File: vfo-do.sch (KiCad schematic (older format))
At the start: 23 parts, among them P1 12V in, P2 DWN, P3 Si5351, P4 Encoder, P5 GPS, P6 UP, P7 Band, P8 Reset, U1 24AA02-OT, U2 LM7808_TO220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

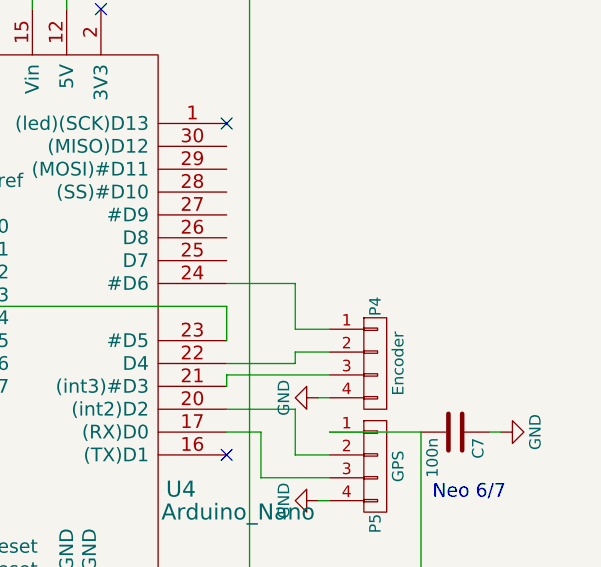
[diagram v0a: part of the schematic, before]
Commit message: Add GPS switchoff button
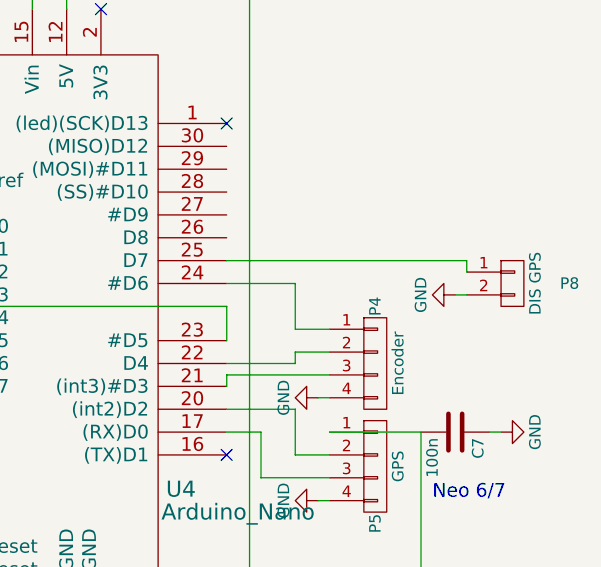
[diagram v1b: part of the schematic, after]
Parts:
- added P8: DIS GPS, Connectors_Molex:Molex_KK-6410-02_02x2.54mm_Straight, symbol vfo-do-rescue:CONN_01X02
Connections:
- net GND: now also P8.2 (P2)
- net at U4.25 (D7): now also P8.1 (P1)
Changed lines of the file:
@@
 Wire Wire Line
 	5800 750  6450 750
+Wire Wire Line
+	9000 3850 9050 3850
+$Comp
+L vfo-do-rescue:CONN_01X02 P8
+U 1 1 613FBEC1
+P 9250 3800
+F 0 "P8" H 9500 3800 50  0000 C CNN
+F 1 "DIS GPS" V 9350 3800 50  0000 C CNN
+F 2 "Connectors_Molex:Molex_KK-6410-02_02x2.54mm_Straight" H 9250 3800 50  0001 C CNN
+F 3 "" H 9250 3800 50  0000 C CNN
+	1    9250 3800
+	1    0    0    -1
+$EndComp
+$Comp
+L vfo-do-rescue:GND #PWR?
+U 1 1 613FBEC7
+P 9000 3850
+F 0 "#PWR?" H 9000 3600 50  0001 C CNN
+F 1 "GND" H 9000 3700 50  0000 C CNN
+F 2 "" H 9000 3850 50  0000 C CNN
+F 3 "" H 9000 3850 50  0000 C CNN
+	1    9000 3850
+	0    1    1    0
+$EndComp
+Wire Wire Line
+	9050 3700 9050 3750
+Wire Wire Line
+	8000 3700 9050 3700
 $EndSCHEMATC
